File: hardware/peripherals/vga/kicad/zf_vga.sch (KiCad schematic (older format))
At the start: 48 parts, among them J2 Z-FIGHTER Expansion Port, J3 DB15_Female, J4 DB9_Male, J5 DB9_Male, SW1 SW_DIP_x03, U1 4040, U10 74HC165, U11 AS6C6264, U12 74HC541, U13 74HC541, U14 74HC541, U2 4040, U3 GAL16V8, U4 GAL16V8, U5 74HC541, U6 74HC541, U7 74HC00, U8 74HC04, U9 74HC74, X1 CXO_DIP14

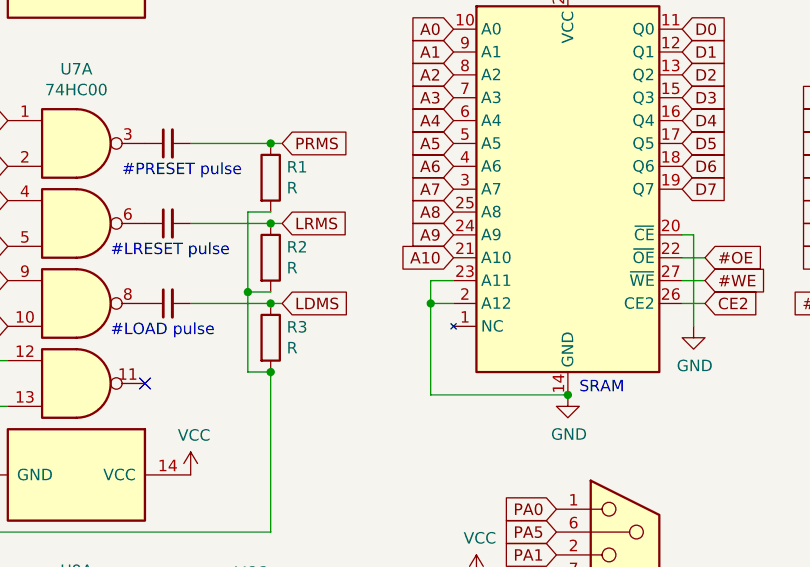
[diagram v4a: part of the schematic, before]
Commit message: Routing draft, changed SRAM NC pin to VCC
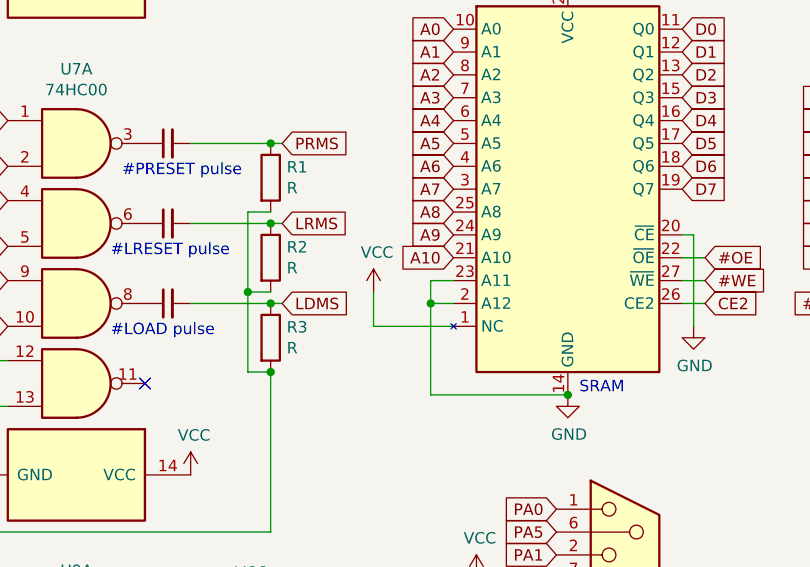
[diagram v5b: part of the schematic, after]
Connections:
- net VCC: now also U11.1 (NC)
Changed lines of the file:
@@
-	1    0    0    -1
-$EndComp
-$Comp
-L Memory_RAM:AS6C6264 U11
-U 1 1 62268A82
-P 7050 4150
-F 0 "U11" H 7050 5231 50  0000 C CNN
-F 1 "AS6C6264" H 7050 5140 50  0000 C CNN
-F 2 "Package_DIP:DIP-28_W15.24mm_LongPads" H 7050 4050 50  0001 C CNN
-F 3 "https://www.futurlec.com/Datasheet/Memory/62256.pdf" H 7050 4050 50  0001 C CNN
-	1    7050 4150
 	1    0    0    -1
 $EndComp
@@
 #RESET
 NoConn ~ 3600 4100
+$Comp
+L Memory_RAM:AS6C6264 U11
+U 1 1 62268A82
+P 7050 4150
+F 0 "U11" H 7050 5231 50  0000 C CNN
+F 1 "AS6C6264" H 7050 5140 50  0000 C CNN
+F 2 "Package_DIP:DIP-28_W15.24mm_LongPads" H 7050 4050 50  0001 C CNN
+F 3 "https://www.futurlec.com/Datasheet/Memory/62256.pdf" H 7050 4050 50  0001 C CNN
+	1    7050 4150
+	1    0    0    -1
+$EndComp
+$Comp
+L power:VCC #PWR?
+U 1 1 6232784E
+P 6200 4600
+F 0 "#PWR?" H 6200 4450 50  0001 C CNN
+F 1 "VCC" H 6215 4773 50  0000 C CNN
+F 2 "" H 6200 4600 50  0001 C CNN
+F 3 "" H 6200 4600 50  0001 C CNN
+	1    6200 4600
+	1    0    0    -1
+$EndComp
+Wire Wire Line
+	6200 4600 6200 4750
+Wire Wire Line
+	6200 4750 6550 4750
 $EndSCHEMATC

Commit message: Routing, silkscreen
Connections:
- net GND: now also U11.1 (NC)
- net VCC: no longer U11.1 (NC)
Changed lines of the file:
@@
 Connection ~ 6450 4650
 Wire Wire Line
-	6450 4650 6450 5050
+	6450 4650 6450 4750
 Text GLabel 2500 6400 0    50   Input ~ 0
 #OE
@@
 	1    0    0    -1
 $EndComp
-$Comp
-L power:VCC #PWR?
-U 1 1 6232784E
-P 6200 4600
-F 0 "#PWR?" H 6200 4450 50  0001 C CNN
-F 1 "VCC" H 6215 4773 50  0000 C CNN
-F 2 "" H 6200 4600 50  0001 C CNN
-F 3 "" H 6200 4600 50  0001 C CNN
-	1    6200 4600
-	1    0    0    -1
-$EndComp
-Wire Wire Line
-	6200 4600 6200 4750
-Wire Wire Line
-	6200 4750 6550 4750
+Wire Wire Line
+	6550 4750 6450 4750
+Connection ~ 6450 4750
+Wire Wire Line
+	6450 4750 6450 5050
 $EndSCHEMATC
